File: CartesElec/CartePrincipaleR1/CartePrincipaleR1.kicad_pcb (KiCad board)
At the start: 2 copper layers, 100 x 100 mm, 27 parts, among them U1 LT1129-3.3_SOT223

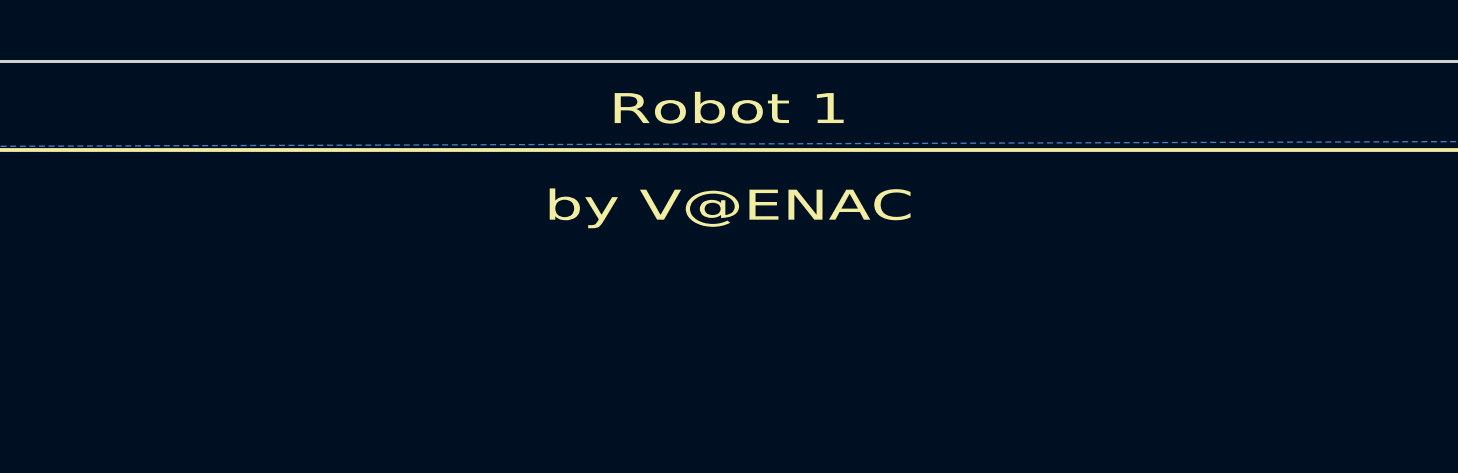
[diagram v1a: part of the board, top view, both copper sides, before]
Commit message: Ajout de la date
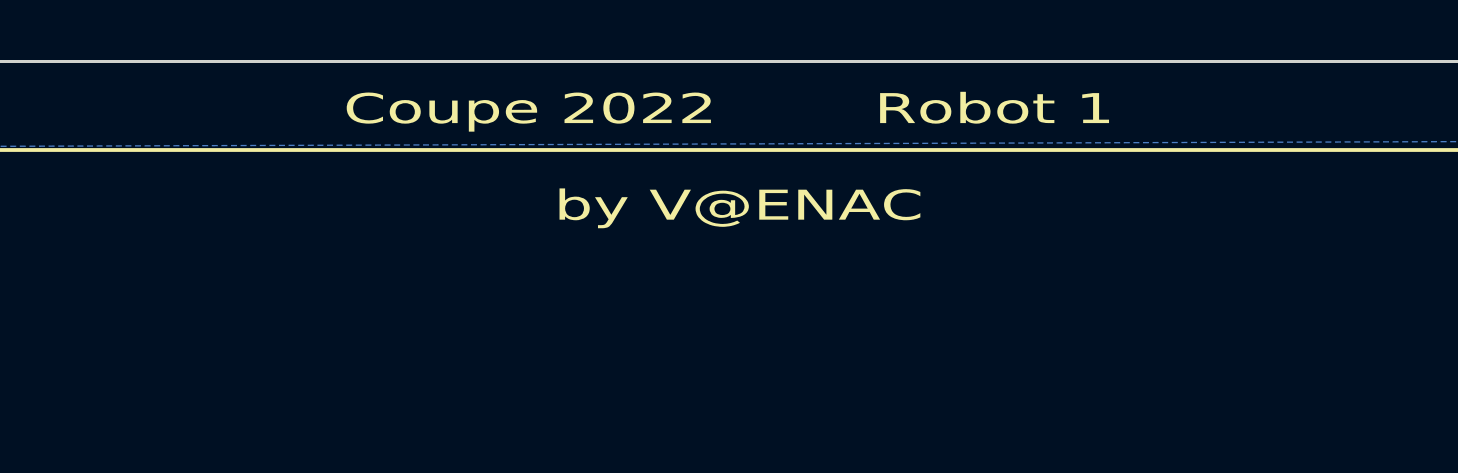
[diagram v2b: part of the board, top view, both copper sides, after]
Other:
- board text added: "Coupe 2022 Robot 1 by V@ENAC"
- board text removed: "Robot 1 by V@ENAC"
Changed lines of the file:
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@@
     (effects (font (size 1 1) (thickness 0.15)))
   )
-  (gr_text "Robot 1\n\nby V@ENAC" (at 105.1 38.2) (layer "F.SilkS")
+  (gr_text "Coupe 2022		Robot 1 \n\n by V@ENAC" (at 105.1 38.2) (layer "F.SilkS")
     (effects (font (size 1 1.5) (thickness 0.15)))
   )
